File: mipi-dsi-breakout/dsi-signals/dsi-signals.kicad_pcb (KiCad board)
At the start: 4 copper layers, 77.4 x 59.6 mm, 21 parts, among them J1 Conn_01x03_Pin, J2 Conn_01x06_Pin, J5 Conn_01x01_Pin

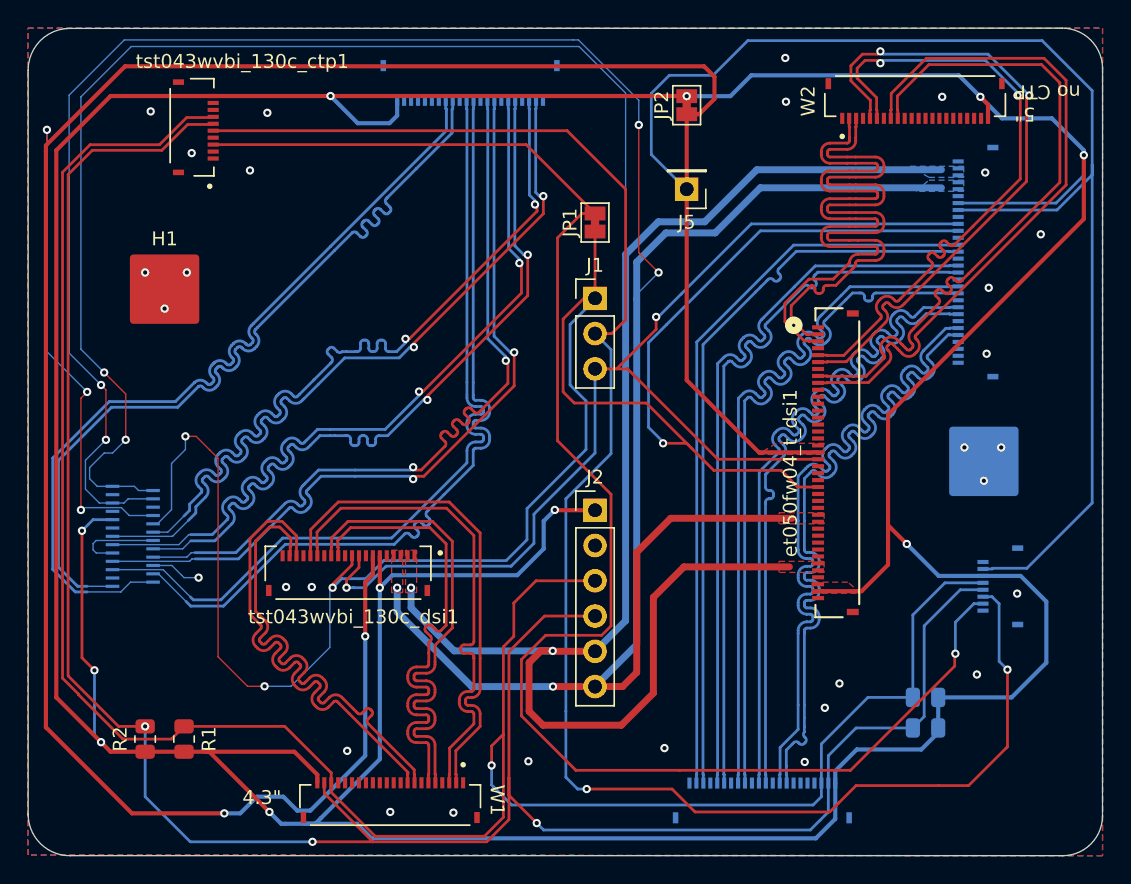
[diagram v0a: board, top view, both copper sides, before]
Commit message: Remove lcd-peripherals and finish second draft of dsi signals.
The LCD peripherals doesn't seem like it adds enough to warrant having a
separate iteration for this pcb. The circuitry from the ap5726 and attiny
projects can hook up to the header pin on the dsi-signals board
directly.

This is a fully routed draft of the dsi signals on a 4 layer PCB.
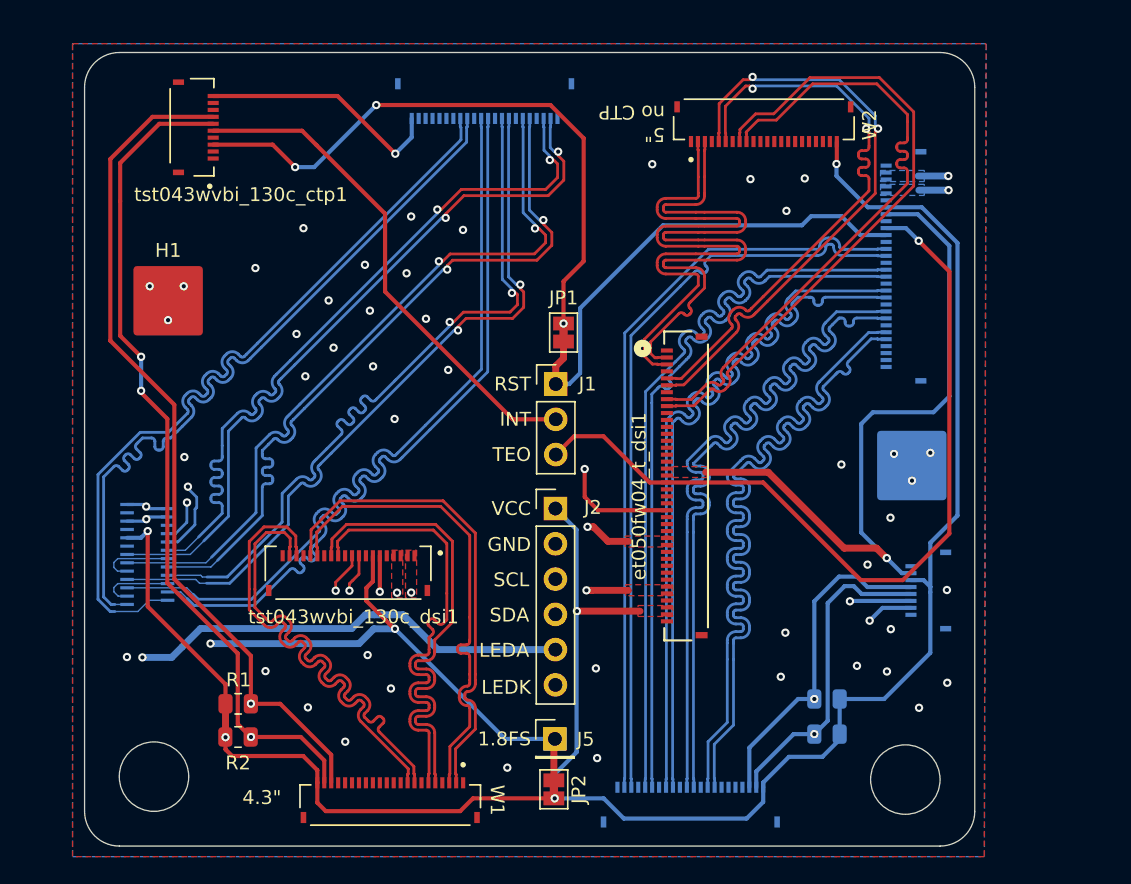
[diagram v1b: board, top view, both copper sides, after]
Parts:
- moved JP2 50.2 mm to (148.8, 132.8), turned to -90 degrees
- moved J5 40.7 mm to (148.9, 129.2), turned to 0 degrees
- moved W2 11.0 mm to (164.0, 84.9)
- moved et050fw04_t_dsi1 11.0 mm to (157.0, 120.7)
- moved JP1 8.24 mm to (149.5, 99.9)
- moved R4 7.11 mm to (168.5, 128.8)
- moved R3 7.10 mm to (168.5, 126.3)
- moved J1 6.79 mm to (149.0, 103.6)
- moved R2 6.69 mm to (126.1, 129.1), turned to 0 degrees
- moved H2 5.20 mm to (174.6, 109.5)
- moved W3 5.20 mm to (158.7, 133.9)
- moved tst050hdbs_80c_ctp1 5.20 mm to (175.7, 118.5)
- moved tst050hdbs_80c_dsi1 5.20 mm to (174.0, 95.2)
- moved R1 4.65 mm to (126.1, 126.7), turned to 0 degrees
- moved J2 2.86 mm to (148.9, 112.6)
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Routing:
- net /1.8_FS: track 299.9 -> 143.7 mm, vias 5 -> 4
- net VCC: track 352.1 -> 225.1 mm, vias 11 -> 7
- net /LED_A: track 193.2 -> 127.5 mm, vias 4 -> 5
- net /LED_K: track 194.0 -> 140.4 mm
- net /INTERRUPT: track 123.9 -> 70.4 mm, vias 2 -> 1
- net /RESET_N: track 147.7 -> 107.4 mm
- net /RESET_FS: track 115.7 -> 85.9 mm, vias 1 -> 4
- net /SDA: track 163.2 -> 142.2 mm, vias 3 -> 4
- net /SCL: track 162.1 -> 150.7 mm, vias 1 -> 2
- net /60_CH2_N: track 59.8 -> 56.2 mm
- net /60_CH2_P: track 59.9 -> 56.2 mm
- net /60_CLK_P: track 56.8 -> 53.3 mm
- net /50_CH1_P: track 46.8 -> 43.3 mm
- net /60_CH3_N: track 59.7 -> 56.2 mm
- net /60_CH3_P: track 59.8 -> 56.3 mm
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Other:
- board size 77.4 x 59.6 mm -> 64.1 x 57.2 mm
- board text added: "1.8FS"
- board text added: "5{dblquote} CTP"
- board text added: "GND"
- board text added: "INT"
- board text added: "LEDA"
- board text added: "LEDK"
- board text added: "RST"
- board text added: "SCL"
- board text added: "SDA"
- board text added: "TEO"
- board text added: "VCC"
- board text removed: "5{dblquote} with CTP"

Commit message: Change jumper silkscreen and hole edgecuts.
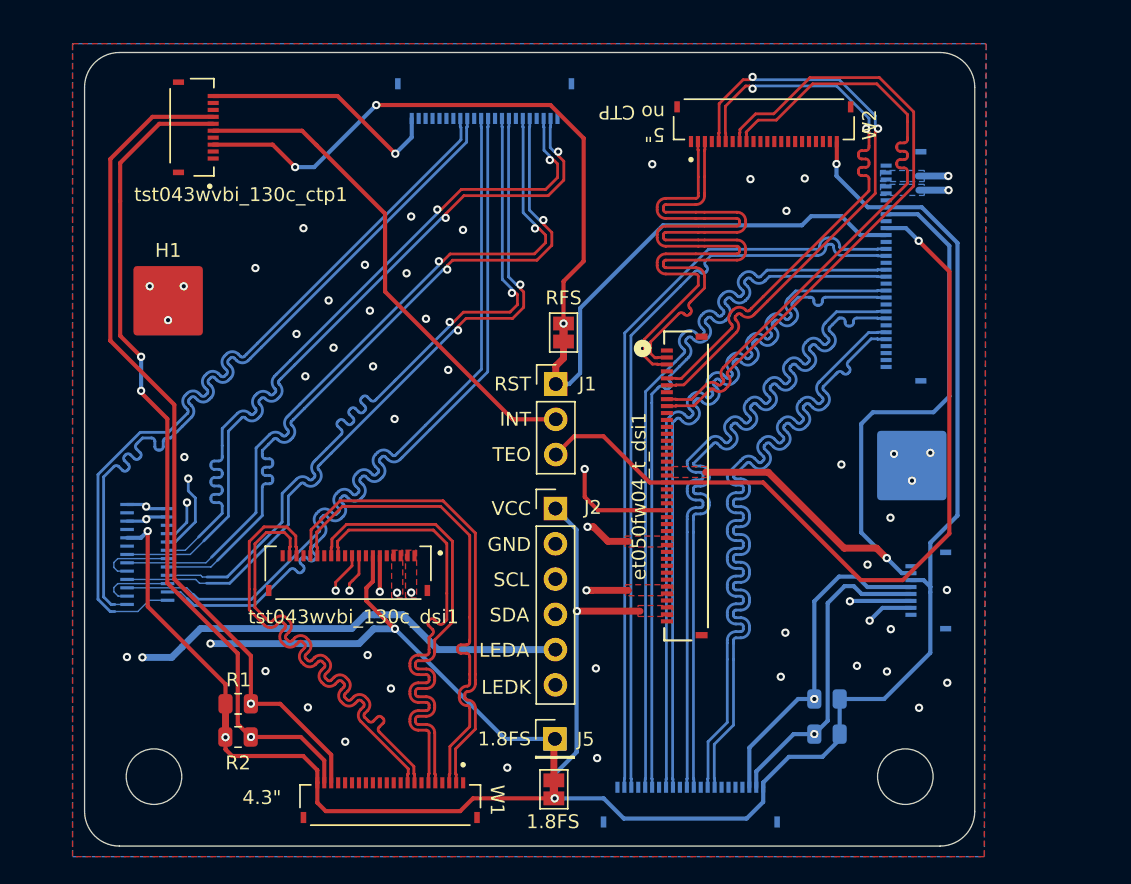
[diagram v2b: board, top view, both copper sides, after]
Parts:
- renumbered JP2 to 1.8FS, JP1 to RFS
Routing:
- net /RESET_N: track 107.4 -> 108.2 mm
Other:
- outline, holes or cut-outs redrawn
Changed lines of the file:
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@@
 		(descr "SMD Solder Jumper, 1x1.5mm Pads, 0.3mm gap, bridged with 1 copper strip")
 		(tags "net tie solder jumper bridged")
-		(property "Reference" "JP1"
+		(property "Reference" "RFS"
 			(at 2.4892 0 180)
 			(layer "F.SilkS")
@@
 		(descr "SMD Solder Jumper, 1x1.5mm Pads, 0.3mm gap, bridged with 1 copper strip")
 		(tags "net tie solder jumper bridged")
-		(property "Reference" "JP2"
-			(at 0 -1.8 90)
+		(property "Reference" "1.8FS"
+			(at 2.3316 0.0666 180)
 			(layer "F.SilkS")
 			(effects
@@
 	(gr_circle
 		(center 120.0366 131.906)
-		(end 122.5366 131.906)
+		(end 122.0366 131.906)
 		(stroke
 			(width 0.05)
@@
 	)
 	(gr_circle
-		(center 174.1462 132.116998)
-		(end 176.6462 132.116998)
+		(center 174.1462 131.906)
+		(end 176.1462 131.906)
 		(stroke
 			(width 0.05)
@@
 	)
 	(via
-		(at 122.4788 111.0234)
+		(at 122.5042 110.4392)
 		(size 0.6)
 		(drill 0.3)
@@
 	)
 	(segment
-		(start 169.545 91.5416)
-		(end 170.905399 92.901999)
-		(width 0.3)
+		(start 122.5042 110.4392)
+		(end 122.5042 111.3282)
+		(width 0.2)
 		(layer "B.Cu")
 		(net 23)
 	)
 	(segment
-		(start 150.7236 98.171)
-		(end 156.6926 92.202)
-		(width 0.3)
+		(start 121.5698 115.0058)
+		(end 121.017 115.0058)
+		(width 0.2)
 		(layer "B.Cu")
 		(net 23)
 	)
 	(segment
-		(start 156.6926 92.202)
-		(end 166.7002 92.202)
+		(start 169.545 91.5416)
+		(end 170.905399 92.901999)
 		(width 0.3)
 		(layer "B.Cu")
@@
 	)
 	(segment
-		(start 149.9362 103.632)
-		(end 150.7236 102.8446)
+		(start 150.7236 98.171)
+		(end 156.6926 92.202)
 		(width 0.3)
 		(layer "B.Cu")
@@
 	)
 	(segment
-		(start 121.017 115.0058)
-		(end 121.7476 115.0058)
+		(start 123.015433 113.560167)
+		(end 121.5698 115.0058)
 		(width 0.2)
 		(layer "B.Cu")
@@
 	)
 	(segment
-		(start 170.905399 92.901999)
-		(end 172.7615 92.901999)
+		(start 156.6926 92.202)
+		(end 166.7002 92.202)
 		(width 0.3)
 		(layer "B.Cu")
@@
 	)
 	(segment
-		(start 123.0122 112.6236)
-		(end 123.1138 112.522)
-		(width 0.2)
+		(start 149.9362 103.632)
+		(end 150.7236 102.8446)
+		(width 0.3)
 		(layer "B.Cu")
 		(net 23)
 	)
 	(segment
-		(start 123.1138 112.522)
-		(end 123.1138 111.7854)
-		(width 0.2)
+		(start 170.905399 92.901999)
+		(end 172.7615 92.901999)
+		(width 0.3)
 		(layer "B.Cu")
 		(net 23)
@@
 	)
 	(segment
-		(start 122.9868 112.649)
-		(end 123.0122 112.6236)
-		(width 0.2)
-		(layer "B.Cu")
-		(net 23)
-	)
-	(segment
-		(start 122.9868 113.7666)
-		(end 122.9868 112.649)
-		(width 0.2)
-		(layer "B.Cu")
-		(net 23)
-	)
-	(segment
-		(start 122.4788 111.1504)
-		(end 122.4788 111.0234)
-		(width 0.2)
-		(layer "B.Cu")
-		(net 23)
-	)
-	(segment
-		(start 121.7476 115.0058)
-		(end 122.9868 113.7666)
+		(start 122.5042 111.3282)
+		(end 123.015433 111.839433)
 		(width 0.2)
 		(layer "B.Cu")
@@
 	)
 	(segment
-		(start 123.1138 111.7854)
-		(end 122.4788 111.1504)
+		(start 123.015433 111.839433)
+		(end 123.015433 113.560167)
 		(width 0.2)
 		(layer "B.Cu")
@@
 	)
 	(segment
-		(start 123.2408 111.5568)
+		(start 123.2408 112.0648)
 		(end 123.2408 119.6086)
 		(width 0.2)
@@
 	)
 	(segment
-		(start 123.2408 119.6086)
-		(end 125.2474 121.6152)
+		(start 122.5042 110.4392)
+		(end 122.5042 111.3282)
 		(width 0.2)
 		(layer "In1.Cu")
@@
 	)
 	(segment
-		(start 125.2474 121.6152)
-		(end 127.9398 124.3076)
+		(start 122.5042 111.3282)
+		(end 123.2408 112.0648)
 		(width 0.2)
 		(layer "In1.Cu")
@@
 	)
 	(segment
-		(start 122.7074 111.0234)
-		(end 123.2408 111.5568)
-		(width 0.2)
-		(layer "In1.Cu")
-		(net 23)
-	)
-	(segment
-		(start 122.4788 111.0234)
-		(end 122.7074 111.0234)
+		(start 123.2408 119.6086)
+		(end 127.9398 124.3076)
 		(width 0.2)
 		(layer "In1.Cu")
